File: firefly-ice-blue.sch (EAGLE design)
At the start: 119 parts, among them J1 USB-5PINZX62WD1-B-5PC, J2 CON-6SOCKET, U1 EFM32LG330F256, U10 STM6519, U11 TPS782XX, U12 TPS6208X, U13 NX3L1T53, U14 FDFMA2P029Z, U16 MEMORY-SPIWLBGA-8, U17 ADP151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

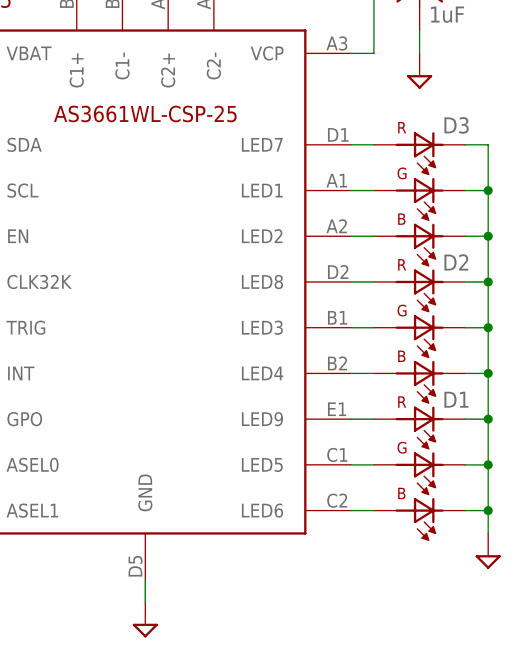
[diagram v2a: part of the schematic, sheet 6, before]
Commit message: add more part info for pricing
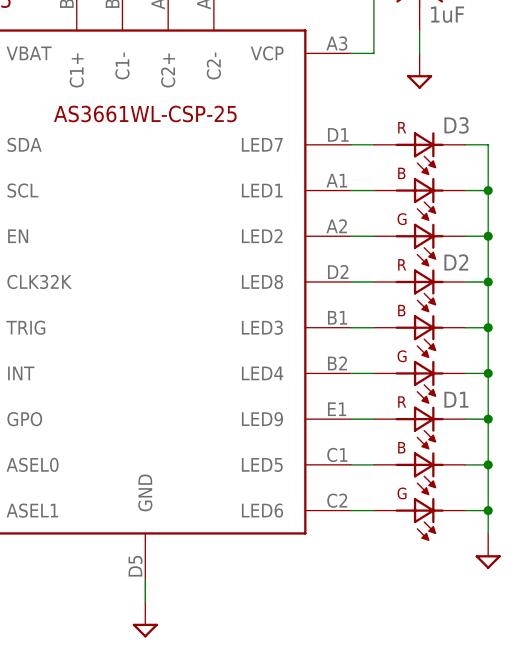
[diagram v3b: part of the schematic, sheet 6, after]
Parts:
- C12, C13, C14, C16, C17, U4: VARIANTS (none) -> magnetometer
- C50, C52: VARIANTS low-power -> color
- C53, C54: MANUFACTURER Samsung Electro-Mechanics America, Inc -> TDK Corporation; ORDERING-CODE CL03A474KQ3NNNC -> C0603X5R0J474M; VARIANTS (none) -> color
- D1, D2, D3, U5: VARIANTS (none) -> color
- J2: DNS true -> (none); VARIANTS (none) -> expansion
- U10: VARIANTS (none) -> failsafe
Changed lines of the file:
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@@
 <attribute name="MANUFACTURER" value="Freescale Semiconductor"/>
 <attribute name="ORDERING-CODE" value="MAG3110FCR1"/>
+<attribute name="VARIANTS" value="magnetometer"/>
 </part>
 <part name="V7" library="firefly" deviceset="GND" device=""/>
@@
 <attribute name="MANUFACTURER" value="Murata"/>
 <attribute name="ORDERING-CODE" value="GRM033R60J104KE19D"/>
+<attribute name="VARIANTS" value="magnetometer"/>
 </part>
 <part name="V15" library="firefly" deviceset="GND" device=""/>
@@
 <attribute name="MANUFACTURER" value="Murata"/>
 <attribute name="ORDERING-CODE" value="GRM033R60J104KE19D"/>
+<attribute name="VARIANTS" value="magnetometer"/>
 </part>
 <part name="V16" library="firefly" deviceset="GND" device=""/>
@@
 <attribute name="MANUFACTURER" value="TDK Corporation"/>
 <attribute name="ORDERING-CODE" value="C0603X5R0J105M030BC"/>
+<attribute name="VARIANTS" value="magnetometer"/>
 </part>
 <part name="V71" library="firefly" deviceset="GND" device=""/>
@@
 <attribute name="MANUFACTURER" value="Murata"/>
 <attribute name="ORDERING-CODE" value="GRM033R60J104KE19D"/>
+<attribute name="VARIANTS" value="magnetometer"/>
 </part>
 <part name="C17" library="firefly" deviceset="C-US" device="C0201" value="100nF">
 <attribute name="MANUFACTURER" value="Murata"/>
 <attribute name="ORDERING-CODE" value="GRM033R60J104KE19D"/>
+<attribute name="VARIANTS" value="magnetometer"/>
 </part>
 <part name="V72" library="firefly" deviceset="GND" device=""/>
@@
 <attribute name="MANUFACTURER" value="Texas Instruments"/>
 <attribute name="ORDERING-CODE" value="LP5523TMX/NOPB"/>
+<attribute name="VARIANTS" value="color"/>
 </part>
 <part name="C50" library="firefly" deviceset="C-US" device="C0201" value="1uF">
 <attribute name="MANUFACTURER" value="TDK Corporation"/>
 <attribute name="ORDERING-CODE" value="C0603X5R0J105M030BC"/>
-<attribute name="VARIANTS" value="low-power"/>
+<attribute name="VARIANTS" value="color"/>
 </part>
 <part name="C52" library="firefly" deviceset="C-US" device="C0201" value="1uF">
 <attribute name="MANUFACTURER" value="TDK Corporation"/>
 <attribute name="ORDERING-CODE" value="C0603X5R0J105M030BC"/>
-<attribute name="VARIANTS" value="low-power"/>
+<attribute name="VARIANTS" value="color"/>
 </part>
 <part name="V94" library="firefly" deviceset="GND" device=""/>
 <part name="C53" library="firefly" deviceset="C-US" device="C0201" value="470nF">
-<attribute name="MANUFACTURER" value="Samsung Electro-Mechanics America, Inc"/>
-<attribute name="ORDERING-CODE" value="CL03A474KQ3NNNC"/>
+<attribute name="MANUFACTURER" value="TDK Corporation"/>
+<attribute name="ORDERING-CODE" value="C0603X5R0J474M"/>
+<attribute name="VARIANTS" value="color"/>
 </part>
 <part name="C54" library="firefly" deviceset="C-US" device="C0201" value="470nF">
-<attribute name="MANUFACTURER" value="Samsung Electro-Mechanics America, Inc"/>
-<attribute name="ORDERING-CODE" value="CL03A474KQ3NNNC"/>
+<attribute name="MANUFACTURER" value="TDK Corporation"/>
+<attribute name="ORDERING-CODE" value="C0603X5R0J474M"/>
+<attribute name="VARIANTS" value="color"/>
 </part>
 <part name="V95" library="firefly" deviceset="GND" device=""/>
@@
 <attribute name="MANUFACTURER" value="STMicroelectronics"/>
 <attribute name="ORDERING-CODE" value="STM6519AHARUB6F"/>
+<attribute name="VARIANTS" value="failsafe"/>
 </part>
 <part name="V53" library="firefly" deviceset="GND" device=""/>
@@
 </part>
 <part name="J2" library="firefly" deviceset="CON-6" device="SOCKET" value="CON-6SOCKET">
-<attribute name="DNS" value="true"/>
 <attribute name="MANUFACTURER" value="Harwin Inc"/>
 <attribute name="ORDERING-CODE" value="M40-3100345R"/>
+<attribute name="VARIANTS" value="expansion"/>
 </part>
 <part name="USBID" library="firefly" deviceset="TARGET-PIN" device=""/>
@@
 <attribute name="MANUFACTURER" value="Rohm Semiconductor"/>
 <attribute name="ORDERING-CODE" value="SMLP36RGB1W3"/>
+<attribute name="VARIANTS" value="color"/>
 </part>
 <part name="D3" library="firefly" deviceset="LED-RGB" device="">
 <attribute name="MANUFACTURER" value="Rohm Semiconductor"/>
 <attribute name="ORDERING-CODE" value="SMLP36RGB1W3"/>
+<attribute name="VARIANTS" value="color"/>
 </part>
 <part name="D2" library="firefly" deviceset="LED-RGB" device="">
 <attribute name="MANUFACTURER" value="Rohm Semiconductor"/>
 <attribute name="ORDERING-CODE" value="SMLP36RGB1W3"/>
+<attribute name="VARIANTS" value="color"/>
 </part>
 <part name="V68" library="firefly" deviceset="GND" device=""/>
@@
 <attribute name="MANUFACTURER" x="134.62" y="101.6" size="1.778" layer="96" display="off"/>
 <attribute name="ORDERING-CODE" x="134.62" y="101.6" size="1.778" layer="96" display="off"/>
+<attribute name="VARIANTS" x="134.62" y="101.6" size="1.778" layer="96" display="off"/>
 </instance>
 <instance part="V7" gate="GND" x="137.16" y="73.66"/>
@@
 <attribute name="MANUFACTURER" x="116.84" y="129.54" size="1.778" layer="96" display="off"/>
 <attribute name="ORDERING-CODE" x="116.84" y="129.54" size="1.778" layer="96" display="off"/>
+<attribute name="VARIANTS" x="116.84" y="129.54" size="1.778" layer="96" display="off"/>
 </instance>
 <instance part="V15" gate="GND" x="116.84" y="119.38"/>
@@
 <attribute name="MANUFACTURER" x="152.4" y="129.54" size="1.778" layer="96" display="off"/>
 <attribute name="ORDERING-CODE" x="152.4" y="129.54" size="1.778" layer="96" display="off"/>
+<attribute name="VARIANTS" x="152.4" y="129.54" size="1.778" layer="96" display="off"/>
 </instance>
 <instance part="V16" gate="GND" x="152.4" y="119.38"/>
@@
 <attribute name="MANUFACTURER" x="165.1" y="129.54" size="1.778" layer="96" display="off"/>
 <attribute name="ORDERING-CODE" x="165.1" y="129.54" size="1.778" layer="96" display="off"/>
+<attribute name="VARIANTS" x="165.1" y="129.54" size="1.778" layer="96" display="off"/>
 </instance>
 <instance part="V71" gate="GND" x="165.1" y="119.38"/>
@@
 <attribute name="MANUFACTURER" x="154.94" y="93.98" size="1.778" layer="96" display="off"/>
 <attribute name="ORDERING-CODE" x="154.94" y="93.98" size="1.778" layer="96" display="off"/>
+<attribute name="VARIANTS" x="154.94" y="93.98" size="1.778" layer="96" display="off"/>
 </instance>
 <instance part="C17" gate="G$1" x="167.64" y="93.98">
 <attribute name="MANUFACTURER" x="167.64" y="93.98" size="1.778" layer="96" display="off"/>
 <attribute name="ORDERING-CODE" x="167.64" y="93.98" size="1.778" layer="96" display="off"/>
+<attribute name="VARIANTS" x="167.64" y="93.98" size="1.778" layer="96" display="off"/>
 </instance>
 <instance part="V72" gate="GND" x="154.94" y="83.82"/>
@@
 <attribute name="ORDERING-CODE" x="134.62" y="177.8" size="1.778" layer="96" display="off"/>
 <attribute name="MANUFACTURER" x="134.62" y="177.8" size="1.778" layer="96" display="off"/>
-<attribute name="DNS" x="134.62" y="177.8" size="1.778" layer="96" display="off"/>
+<attribute name="VARIANTS" x="134.62" y="177.8" size="1.778" layer="96" display="off"/>
 </instance>
 </instances>
@@
 <attribute name="MANUFACTURER" x="93.98" y="149.86" size="1.778" layer="96" display="off"/>
 <attribute name="ORDERING-CODE" x="93.98" y="149.86" size="1.778" layer="96" display="off"/>
+<attribute name="VARIANTS" x="93.98" y="149.86" size="1.778" layer="96" display="off"/>
 </instance>
 <instance part="C50" gate="G$1" x="60.96" y="182.88">
@@
 <attribute name="ORDERING-CODE" x="83.82" y="193.04" size="1.778" layer="96" rot="R90" display="off"/>
 <attribute name="MANUFACTURER" x="83.82" y="193.04" size="1.778" layer="96" rot="R90" display="off"/>
+<attribute name="VARIANTS" x="83.82" y="193.04" size="1.778" layer="96" rot="R90" display="off"/>
 </instance>
 <instance part="C54" gate="G$1" x="101.6" y="193.04" rot="R90">
 <attribute name="ORDERING-CODE" x="101.6" y="193.04" size="1.778" layer="96" rot="R90" display="off"/>
 <attribute name="MANUFACTURER" x="101.6" y="193.04" size="1.778" layer="96" rot="R90" display="off"/>
+<attribute name="VARIANTS" x="101.6" y="193.04" size="1.778" layer="96" rot="R90" display="off"/>
 </instance>
 <instance part="V95" gate="GND" x="68.58" y="119.38"/>
@@
 <attribute name="ORDERING-CODE" x="124.46" y="129.54" size="1.778" layer="96" display="off"/>
 <attribute name="MANUFACTURER" x="124.46" y="129.54" size="1.778" layer="96" display="off"/>
+<attribute name="VARIANTS" x="124.46" y="129.54" size="1.778" layer="96" display="off"/>
 </instance>
 <instance part="D3" gate="G$1" x="124.46" y="160.02">
 <attribute name="ORDERING-CODE" x="124.46" y="160.02" size="1.778" layer="96" display="off"/>
 <attribute name="MANUFACTURER" x="124.46" y="160.02" size="1.778" layer="96" display="off"/>
+<attribute name="VARIANTS" x="124.46" y="160.02" size="1.778" layer="96" display="off"/>
 </instance>
 <instance part="D2" gate="G$1" x="124.46" y="144.78">
 <attribute name="ORDERING-CODE" x="124.46" y="144.78" size="1.778" layer="96" display="off"/>
 <attribute name="MANUFACTURER" x="124.46" y="144.78" size="1.778" layer="96" display="off"/>
+<attribute name="VARIANTS" x="124.46" y="144.78" size="1.778" layer="96" display="off"/>
 </instance>
 <instance part="V68" gate="GND" x="132.08" y="119.38"/>
@@
 <attribute name="ORDERING-CODE" x="60.96" y="114.3" size="1.778" layer="96" display="off"/>
 <attribute name="MANUFACTURER" x="60.96" y="114.3" size="1.778" layer="96" display="off"/>
+<attribute name="VARIANTS" x="60.96" y="114.3" size="1.778" layer="96" display="off"/>
 </instance>
 <instance part="R4" gate="G$1" x="210.82" y="81.28" rot="R270">

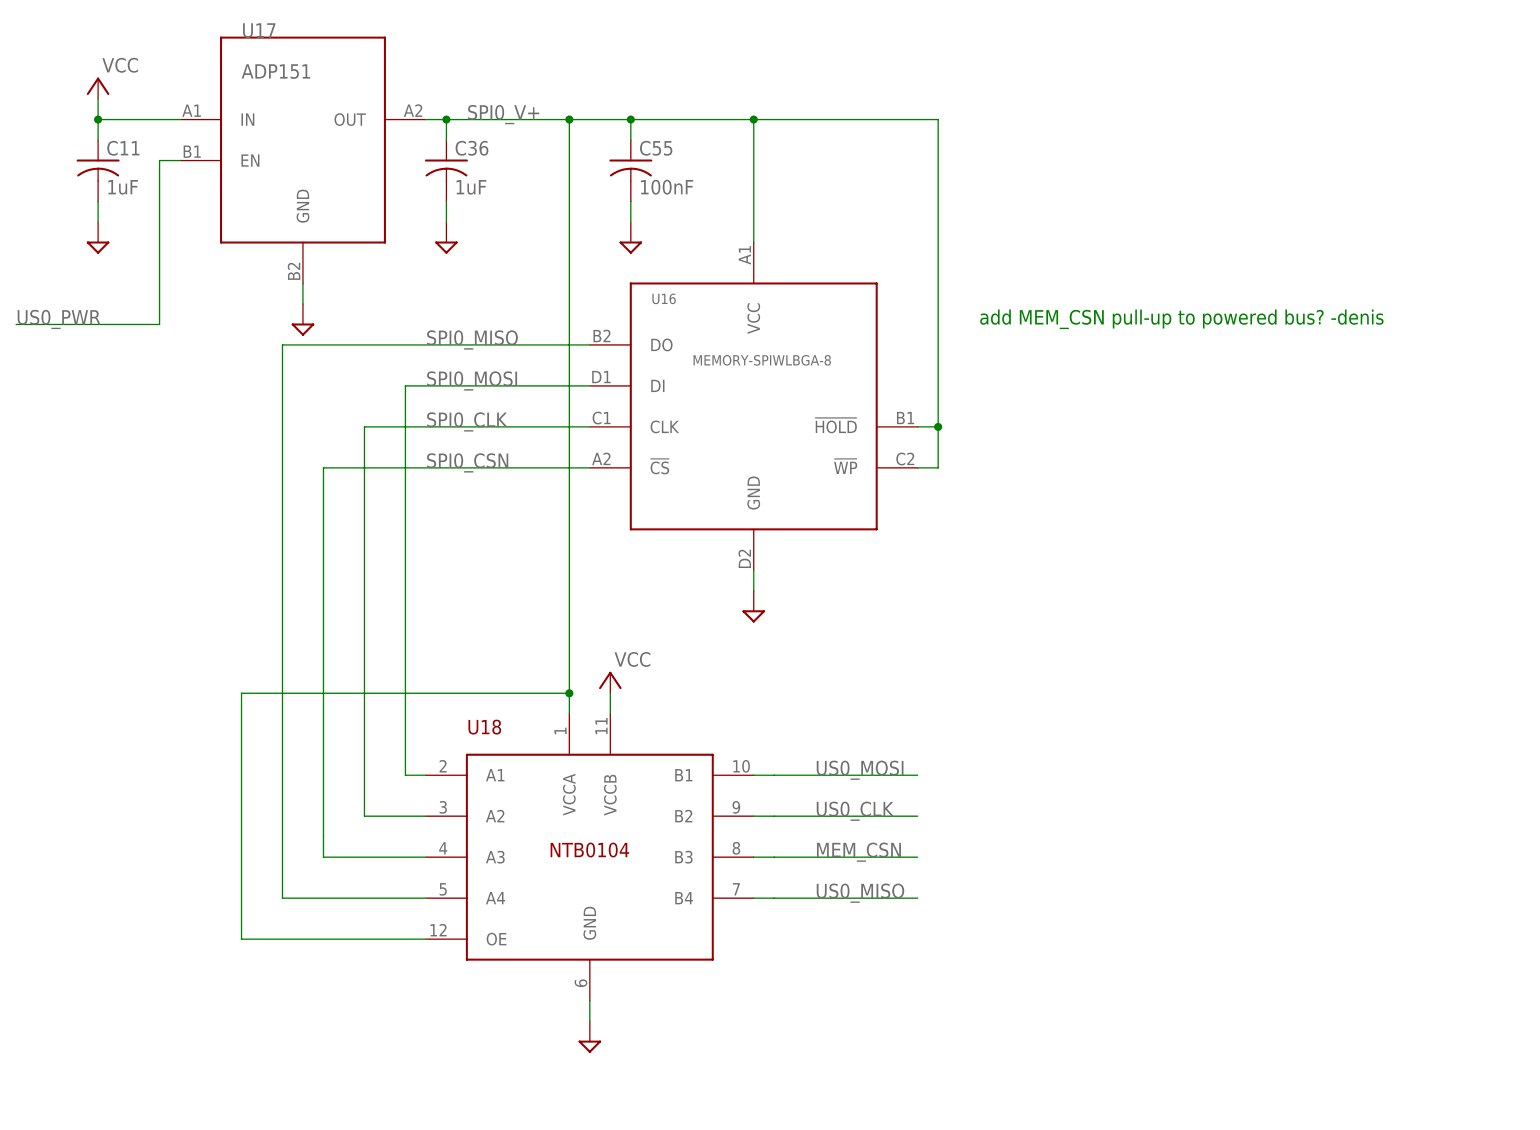
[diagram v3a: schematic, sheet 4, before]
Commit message: fix power/ground short in USB connector mounting posts; fix MOSI/MISO to memory and add chip select pullup
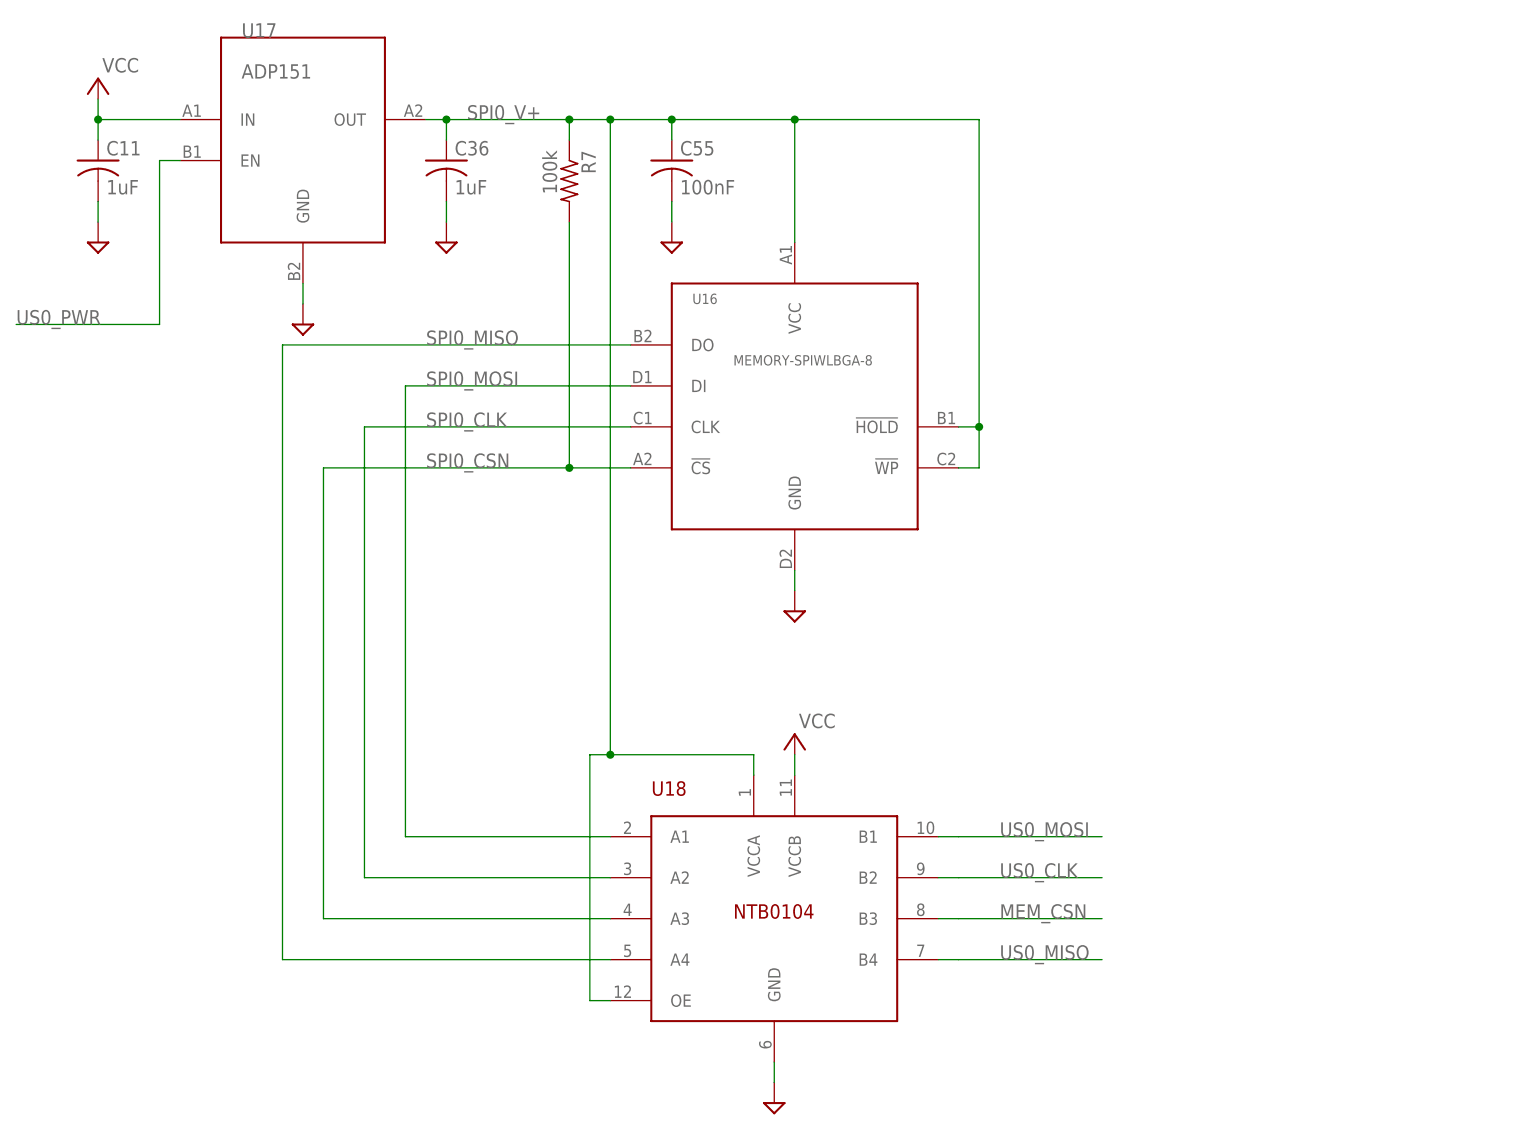
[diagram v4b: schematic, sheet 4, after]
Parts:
- added R7: 100k, firefly:R-US_R0201
- C18, C25: ORDERING-CODE CL05A106MQ5NUNC -> CL05A106MP5NUNC
- D1, D2, D3: ORDERING-CODE SMLP36RGB1W3 -> SMLP36RGB2W3
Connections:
- net SPI0_CSN: now also R7.2
- net SPI0_V+: now also R7.1
- net US0_MISO: now also U1E.PE11/LES_ALTEX5/TIM1_CC1#1/US0_RX#0; no longer U1E.PE10/TIM1_CC0#1/US0_TX#0
- net US0_MOSI: now also U1E.PE10/TIM1_CC0#1/US0_TX#0; no longer U1E.PE11/LES_ALTEX5/TIM1_CC1#1/US0_RX#0
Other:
- note removed: "add MEM_CSN pull-up to powered bus? -denis"
- moved on the sheet: C55, U16, U18
